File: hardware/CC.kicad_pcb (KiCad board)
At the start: 2 copper layers, 75 x 34 mm, 46 parts, among them J1 Conn_01x02_Female, J2 Conn_02x20_Odd_Even, Q1 Q_DUAL_NPN, SW1 SW-2P, U1 CH9328, U2 CP2102N-A01-GQFN28, U3 ESP32-WROOM-32D, U4 AMS1117-3.3, U5 BL1530-DPDT

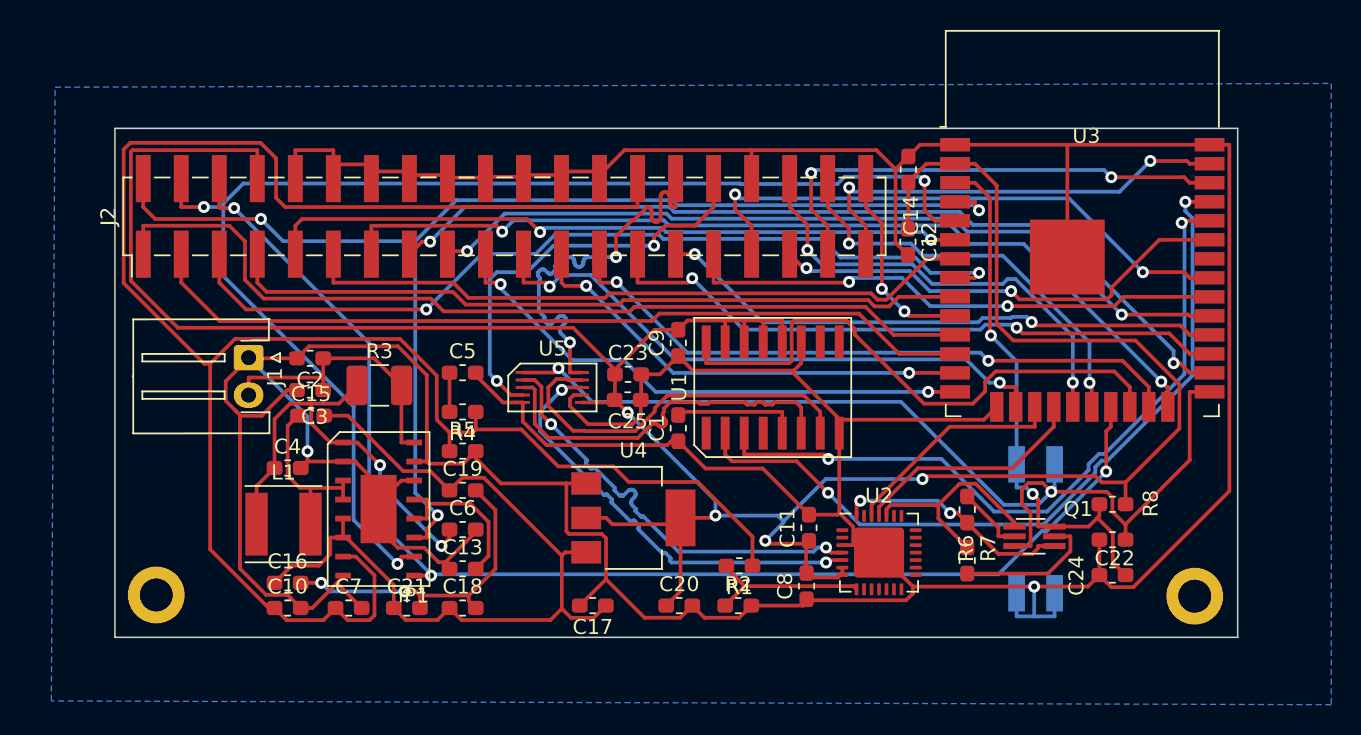
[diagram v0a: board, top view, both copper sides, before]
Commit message: feat(hardware): update the ip5206 to ip5108 and change the bl1530 footprint
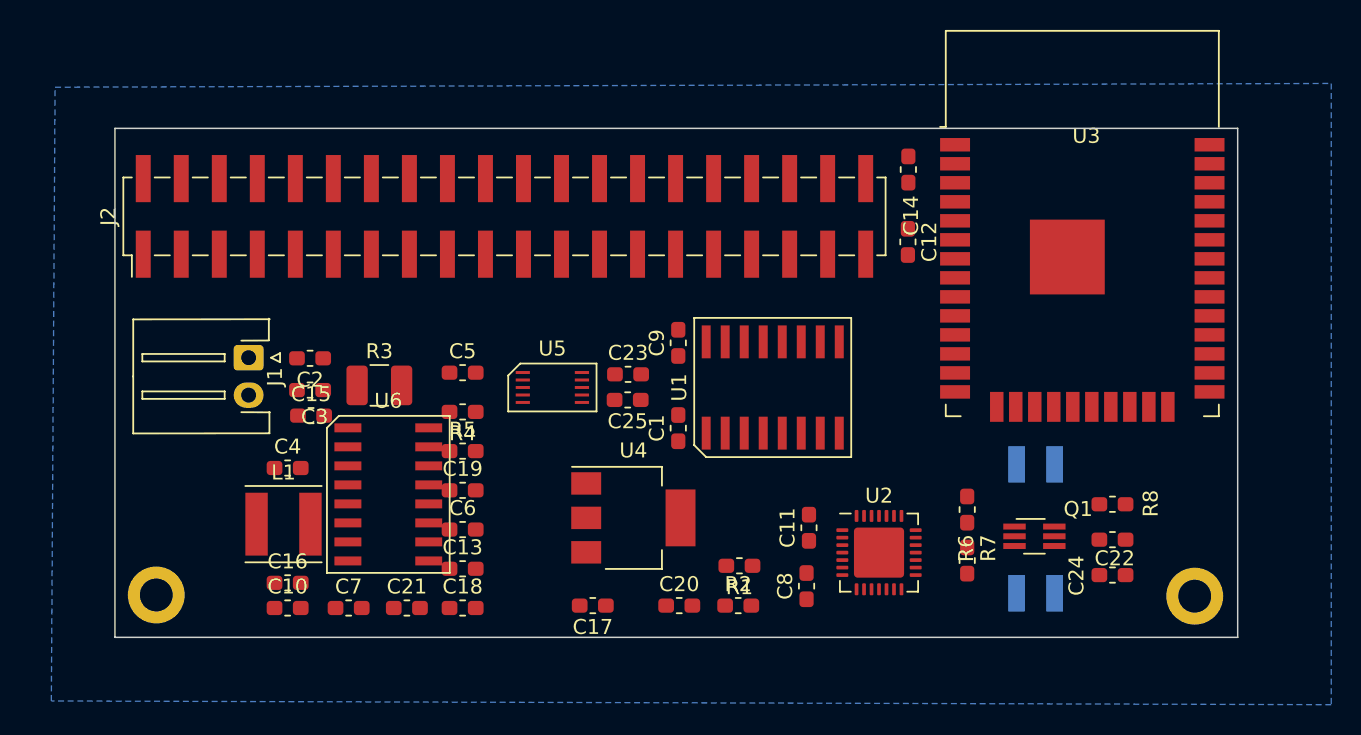
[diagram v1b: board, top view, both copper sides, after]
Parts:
- removed IP1: IP5206, keyboard:IP5206
- added U6: IP5108, keyboard:IP5108, F.Cu at (48.3, 44.5)
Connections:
- U1 pad 1: (no net) -> Net-(U1-Pad1)
- U1 pad 10: (no net) -> Net-(U1-Pad10)
- U1 pad 4: (no net) -> Net-(U1-Pad4)
- U1 pad 9: (no net) -> Net-(U1-Pad9)
- U2 pad 1: (no net) -> Net-(U2-Pad1)
- U2 pad 10: (no net) -> Net-(U2-Pad10)
- U2 pad 11: (no net) -> Net-(U2-Pad11)
- U2 pad 12: (no net) -> Net-(U2-Pad12)
- U2 pad 13: (no net) -> Net-(U2-Pad13)
- U2 pad 14: (no net) -> Net-(U2-Pad14)
- U2 pad 15: (no net) -> Net-(U2-Pad15)
- U2 pad 16: (no net) -> Net-(U2-Pad16)
- U2 pad 17: (no net) -> Net-(U2-Pad17)
- U2 pad 18: (no net) -> Net-(U2-Pad18)
- U2 pad 19: (no net) -> Net-(U2-Pad19)
- U2 pad 2: (no net) -> Net-(U2-Pad2)
- U2 pad 20: (no net) -> Net-(U2-Pad20)
- U2 pad 21: (no net) -> Net-(U2-Pad21)
- U2 pad 22: (no net) -> Net-(U2-Pad22)
- U2 pad 23: (no net) -> Net-(U2-Pad23)
- U2 pad 27: (no net) -> Net-(U2-Pad27)
- U2 pad 9: (no net) -> Net-(U2-Pad9)
- U3 pad 32: (no net) -> Net-(U3-Pad32)
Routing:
- net GND: track 352.9 -> 0.00 mm, vias 2 -> 0
- net VDD33: track 183.6 -> 0.00 mm, vias 4 -> 0
- net VBUS: track 136.7 -> 0.00 mm
- net /L2: track 87.1 -> 0.00 mm, vias 3 -> 0
- net /L1: track 86.4 -> 0.00 mm, vias 3 -> 0
- net /L3: track 83.7 -> 0.00 mm, vias 3 -> 0
- net /IO0: track 68.4 -> 0.00 mm, vias 2 -> 0
- net /COL1: track 61.5 -> 0.00 mm, vias 2 -> 0
- net /ROW1: track 60.9 -> 0.00 mm
- net /COL2: track 59.8 -> 0.00 mm, vias 2 -> 0
- net /ROW3: track 58.3 -> 0.00 mm, vias 2 -> 0
- net /ROW2: track 56.0 -> 0.00 mm
- net VDD5V: track 55.8 -> 0.00 mm
- net /COL3: track 54.9 -> 0.00 mm, vias 2 -> 0
- net /KTXD: track 52.3 -> 0.00 mm, vias 2 -> 0
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
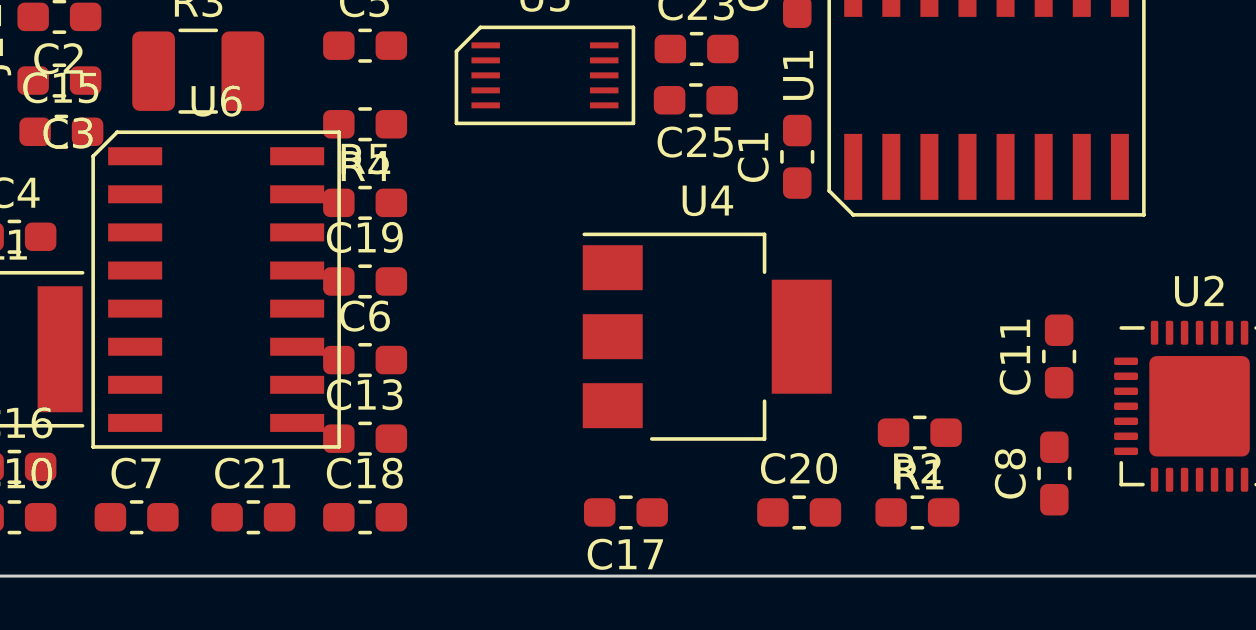
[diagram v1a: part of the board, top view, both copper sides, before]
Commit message: feat: add qfn 28
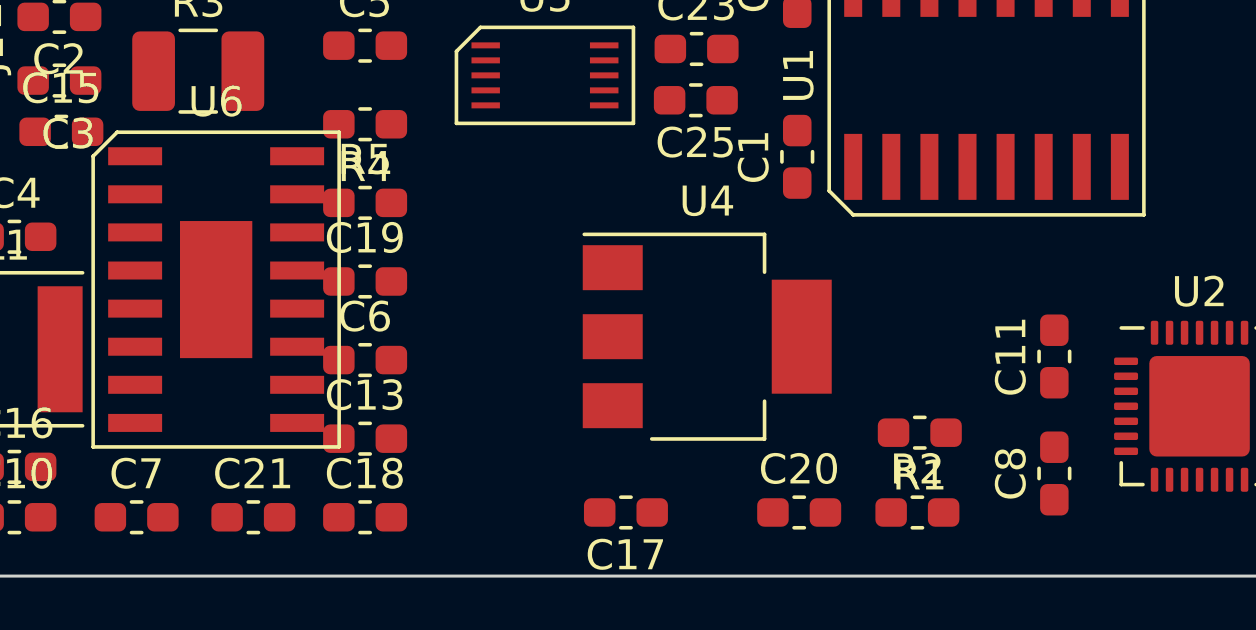
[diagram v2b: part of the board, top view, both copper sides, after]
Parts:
- moved C11 0.16 mm to (76.2, 46.7)

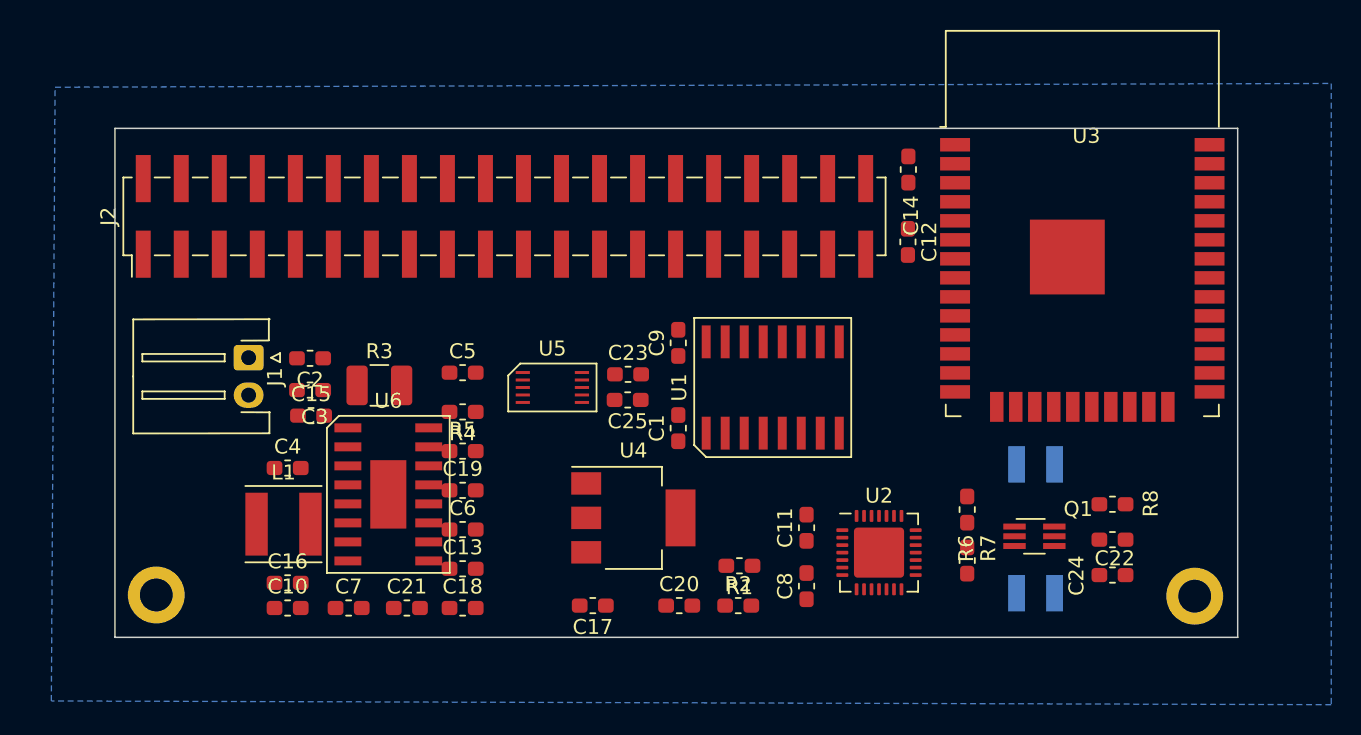
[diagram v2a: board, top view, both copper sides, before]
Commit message: feat(hardward): add quad flat package 28 for cp2102
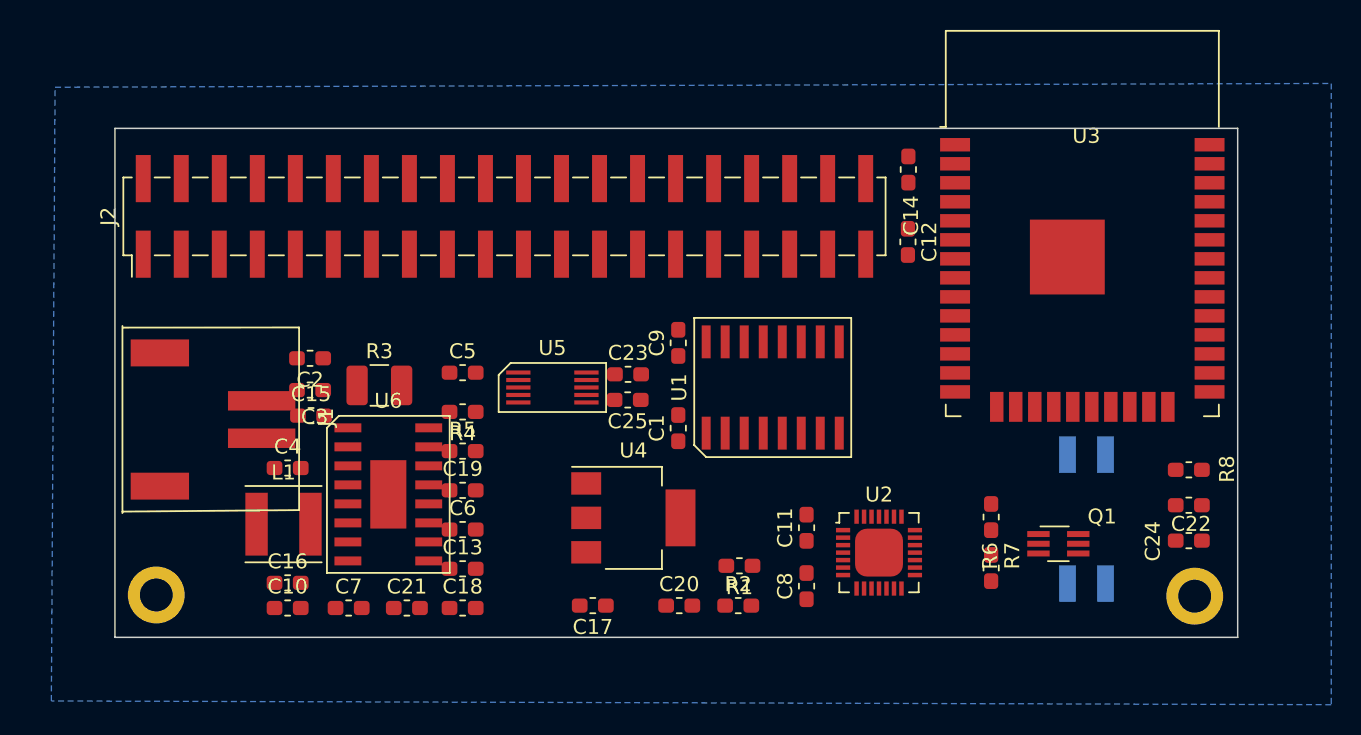
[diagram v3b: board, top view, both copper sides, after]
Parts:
- U2: footprint Package_DFN_QFN:QFN-28-1EP_5x5mm_P0.5mm_EP3.35x3.35mm -> keyboard:QFP-28_5x5_Pitch0.5mm
- U5: footprint keyboard:BL1530—DPDT -> keyboard:BL1530
- moved C22 5.59 mm to (101.7, 45.2)
- moved C24 5.59 mm to (101.7, 47.5)
- moved R8 5.59 mm to (101.7, 42.8)
- moved SW1 3.46 mm to (94.9, 46.1)
- moved J1 3.01 mm to (39.8, 38.2)
- moved Q1 1.68 mm to (93.0, 47.8)
- moved R6 1.68 mm to (88.5, 46.0)
- moved R7 1.68 mm to (88.5, 49.4)
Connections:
- U1 pad 1: Net-(U1-Pad1) -> (no net)
- U1 pad 10: Net-(U1-Pad10) -> (no net)
- U1 pad 4: Net-(U1-Pad4) -> (no net)
- U1 pad 9: Net-(U1-Pad9) -> (no net)
- U2 pad 1: Net-(U2-Pad1) -> (no net)
- U2 pad 10: Net-(U2-Pad10) -> (no net)
- U2 pad 11: Net-(U2-Pad11) -> (no net)
- U2 pad 12: Net-(U2-Pad12) -> (no net)
- U2 pad 13: Net-(U2-Pad13) -> (no net)
- U2 pad 14: Net-(U2-Pad14) -> (no net)
- U2 pad 15: Net-(U2-Pad15) -> (no net)
- U2 pad 16: Net-(U2-Pad16) -> (no net)
- U2 pad 17: Net-(U2-Pad17) -> (no net)
- U2 pad 18: Net-(U2-Pad18) -> (no net)
- U2 pad 19: Net-(U2-Pad19) -> (no net)
- U2 pad 2: Net-(U2-Pad2) -> (no net)
- U2 pad 20: Net-(U2-Pad20) -> (no net)
- U2 pad 21: Net-(U2-Pad21) -> (no net)
- U2 pad 22: Net-(U2-Pad22) -> (no net)
- U2 pad 23: Net-(U2-Pad23) -> (no net)
- U2 pad 27: Net-(U2-Pad27) -> (no net)
- U2 pad 9: Net-(U2-Pad9) -> (no net)
- U3 pad 32: Net-(U3-Pad32) -> (no net)

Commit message: feat: update cc layout
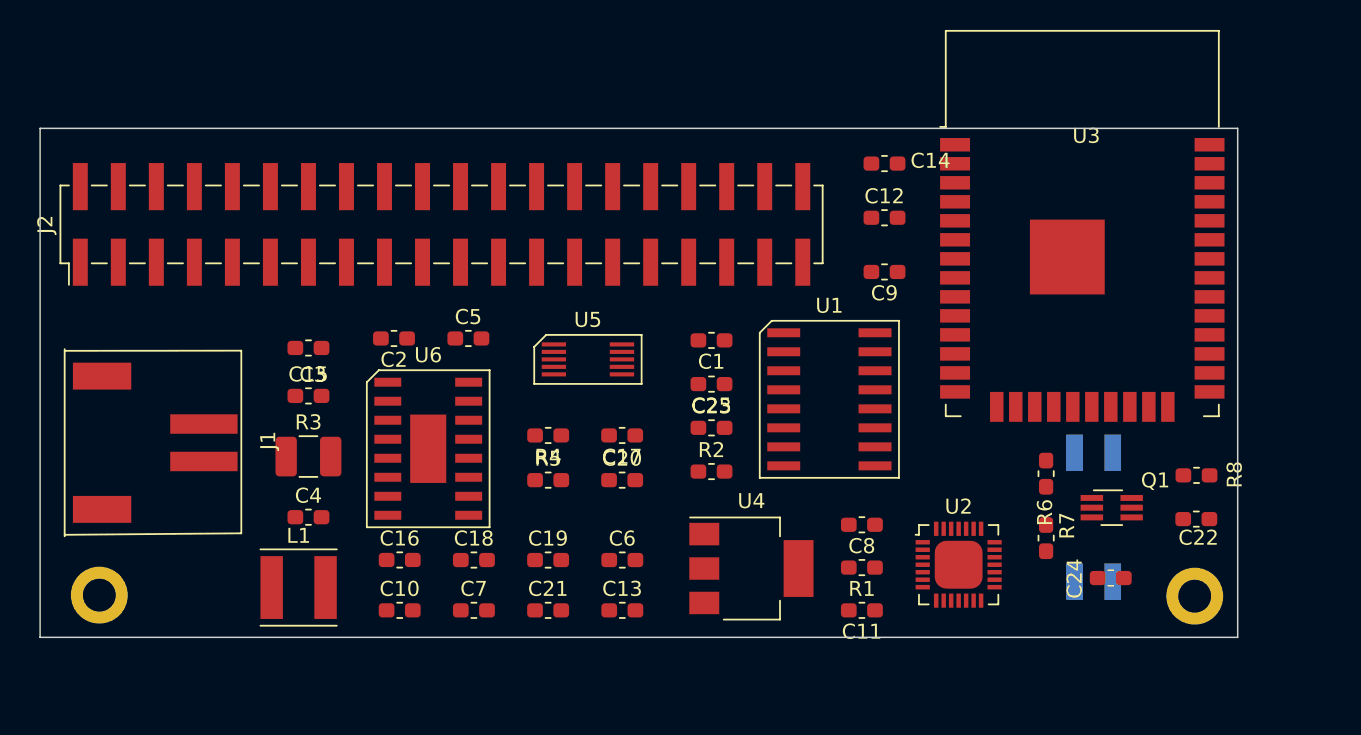
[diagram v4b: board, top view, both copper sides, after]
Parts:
- moved C9 14.6 mm to (81.4, 29.6), turned to 180 degrees
- moved C17 11.5 mm to (63.9, 40.5)
- moved C13 11.0 mm to (63.9, 52.2)
- moved C6 10.9 mm to (63.9, 48.8)
- moved C21 9.44 mm to (58.9, 52.2)
- moved C20 9.21 mm to (63.9, 43.5)
- moved R2 9.13 mm to (69.8, 42.9)
- moved U4 8.58 mm to (72.5, 49.4)
- moved C7 8.37 mm to (54.0, 52.2)
- moved R1 8.18 mm to (79.9, 49.3)
- moved C16 7.64 mm to (49.0, 48.8)
- moved C10 7.49 mm to (49.0, 52.2)
- moved C19 7.37 mm to (58.9, 48.8)
- moved R3 6.71 mm to (42.9, 41.9)
- moved C11 6.64 mm to (79.9, 52.2), turned to 180 degrees
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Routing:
- removed copper zone on B.Cu, net GND
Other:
- board size 75 x 34 mm -> 80 x 34 mm
